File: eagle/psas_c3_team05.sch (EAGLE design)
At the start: 92 parts, among them IC1 CP2102, J1 3220-10-0100-00, J2 1.27MM_HDR_2X12X1, U1 MIC5319 3.3V, U2 MCP73871, U3 MKW01Z128, X1 32 MHz

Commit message: added attributes to battery connector, tri color LEDS
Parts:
- JP1: DIST (none) -> Digi-Key; DPN (none) -> 455-1749-1-ND; MFG (none) -> JST Sales America Inc.; MFG-PN (none) -> S2B-PH-SM4-TB(LF)(SN)
- LED1, LED2: DIST (none) -> Digi-Key; DPN 754-1100-1-ND -> 160-2022-1-ND; MFG (none) -> Lite-On Inc.; MFG-PN (none) -> LTST-C19FD1WT
- LED3: DIST (none) -> Digi-Key; MFG (none) -> Lite-On Inc.; MFG-PN (none) -> LTST-C191KGKT
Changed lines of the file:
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@@
 <attribute name="MFG-PN" value="MIC5319-3.3YD5-TR"/>
 </part>
-<part name="JP1" library="Vibrogait_prototype" deviceset="SPARKFUN-CONNECTORS_M02" device="4UCON-15767" value="BC"/>
+<part name="JP1" library="Vibrogait_prototype" deviceset="SPARKFUN-CONNECTORS_M02" device="4UCON-15767" value="BC">
+<attribute name="DIST" value="Digi-Key"/>
+<attribute name="DPN" value="455-1749-1-ND"/>
+<attribute name="MFG" value="JST Sales America Inc."/>
+<attribute name="MFG-PN" value="S2B-PH-SM4-TB(LF)(SN)"/>
+</part>
 <part name="GND1" library="Vibrogait_prototype" deviceset="GND" device=""/>
 <part name="RT1" library="Vibrogait_prototype" deviceset="THERMISTOR-" device="_1206" value="10K (NTC)">
@@
 <part name="GND25" library="Vibrogait_prototype" deviceset="GND" device=""/>
 <part name="LED1" library="Vibrogait_prototype" deviceset="LED_RGB_COMMON_ANODE-*" device="1.6X1.26" value="APHFT1612PBASURKVGAC">
-<attribute name="DPN" value="754-1100-1-ND"/>
+<attribute name="DIST" value="Digi-Key"/>
+<attribute name="DPN" value="160-2022-1-ND"/>
+<attribute name="MFG" value="Lite-On Inc."/>
+<attribute name="MFG-PN" value="LTST-C19FD1WT"/>
 </part>
 <part name="R3" library="rcl_custom" deviceset="R-US_" device="0603-B-NOSILK" value="1k">
@@
 <part name="TP18" library="microbuilder" deviceset="TESTPOINT" device="ROUND0.5MM"/>
 <part name="LED2" library="Vibrogait_prototype" deviceset="LED_RGB_COMMON_ANODE-*" device="1.6X1.26" value="APHFT1612PBASURKVGAC">
-<attribute name="DPN" value="754-1100-1-ND"/>
+<attribute name="DIST" value="Digi-Key"/>
+<attribute name="DPN" value="160-2022-1-ND"/>
+<attribute name="MFG" value="Lite-On Inc."/>
+<attribute name="MFG-PN" value="LTST-C19FD1WT"/>
 </part>
 <part name="LED3" library="Vibrogait_prototype" deviceset="LED" device="-0603" value="GRN">
+<attribute name="DIST" value="Digi-Key"/>
 <attribute name="DPN" value="160-1446-1-ND"/>
+<attribute name="MFG" value="Lite-On Inc."/>
+<attribute name="MFG-PN" value="LTST-C191KGKT"/>
 </part>
 <part name="R2" library="rcl_custom" deviceset="R-US_" device="0603-B-NOSILK" value="1k">
@@
 <attribute name="VALUE" x="347.98" y="332.74" size="1.778" layer="96" rot="MR0"/>
 <attribute name="NAME" x="347.98" y="343.662" size="1.778" layer="95" rot="MR0"/>
+<attribute name="DIST" x="345.44" y="337.82" size="1.778" layer="96" rot="MR0" display="off"/>
+<attribute name="DPN" x="345.44" y="337.82" size="1.778" layer="96" rot="MR0" display="off"/>
+<attribute name="MFG" x="345.44" y="337.82" size="1.778" layer="96" rot="MR0" display="off"/>
+<attribute name="MFG-PN" x="345.44" y="337.82" size="1.778" layer="96" rot="MR0" display="off"/>
 </instance>
 <instance part="GND1" gate="1" x="337.82" y="307.34" smashed="yes">
@@
 <attribute name="VALUE" x="210.82" y="320.04" size="1.778" layer="96"/>
 <attribute name="DPN" x="213.36" y="309.88" size="1.778" layer="96" rot="MR270" display="off"/>
+<attribute name="DIST" x="213.36" y="309.88" size="1.778" layer="96" rot="MR270" display="off"/>
+<attribute name="MFG" x="213.36" y="309.88" size="1.778" layer="96" rot="MR270" display="off"/>
+<attribute name="MFG-PN" x="213.36" y="309.88" size="1.778" layer="96" rot="MR270" display="off"/>
 </instance>
 <instance part="R3" gate="R" x="226.06" y="314.96" smashed="yes" rot="MR0">
@@
 <attribute name="VALUE" x="76.2" y="233.68" size="1.778" layer="96"/>
 <attribute name="DPN" x="119.38" y="233.68" size="1.778" layer="96" rot="MR0" display="off"/>
+<attribute name="DIST" x="119.38" y="233.68" size="1.778" layer="96" rot="MR0" display="off"/>
+<attribute name="MFG" x="119.38" y="233.68" size="1.778" layer="96" rot="MR0" display="off"/>
+<attribute name="MFG-PN" x="119.38" y="233.68" size="1.778" layer="96" rot="MR0" display="off"/>
 </instance>
 <instance part="LED3" gate="LED" x="477.52" y="345.44" smashed="yes">
@@
 <attribute name="VALUE" x="480.06" y="344.17" size="1.778" layer="96"/>
 <attribute name="DPN" x="477.52" y="345.44" size="1.778" layer="96" display="off"/>
+<attribute name="DIST" x="477.52" y="345.44" size="1.778" layer="96" display="off"/>
+<attribute name="MFG" x="477.52" y="345.44" size="1.778" layer="96" display="off"/>
+<attribute name="MFG-PN" x="477.52" y="345.44" size="1.778" layer="96" display="off"/>
 </instance>
 <instance part="R2" gate="R" x="477.52" y="337.82" smashed="yes" rot="R90">

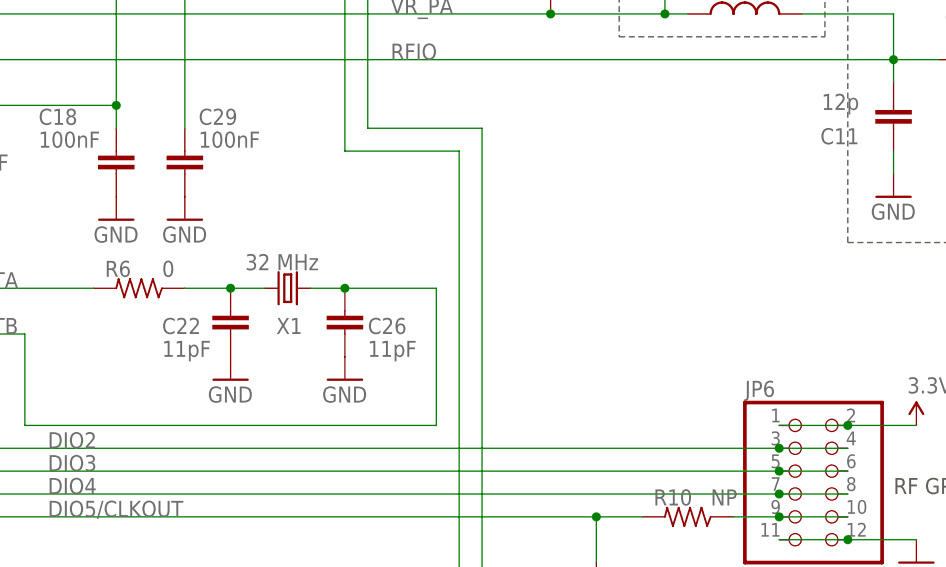
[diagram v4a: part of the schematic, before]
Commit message: added more attributes for part numbers, duplicated crystal because crystal footprint is wrong on the board and we will need to order two just in case things go wrong with the first, hopefully one of the two work lol
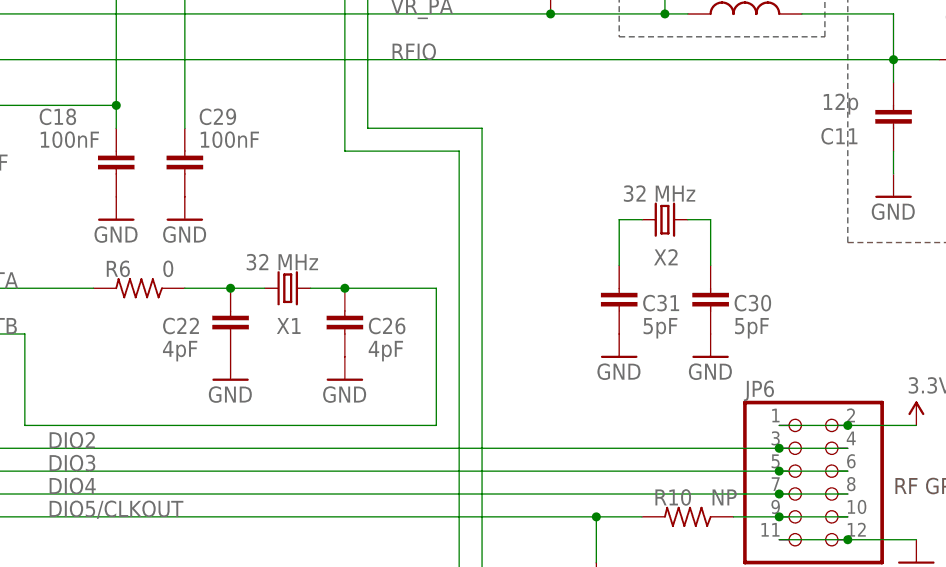
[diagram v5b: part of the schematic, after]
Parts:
- added C30, C31: 5pF, Vibrogait_prototype:C-EU0603-B-NOSILK
- added X2: 32 MHz, crystal:FC-12M
- C22, C26: value 11pF -> 4pF; DPN 490-1532-1-ND -> 490-10720-6-ND; MPN GRM188R71C104KA01D -> GRM1885C1H4R0CA01D
- X1: DPN2 CTX1364CT-ND -> (none); MFG2 CTS-Frequency Controls -> (none); MFG2-PN 402F3201XIAR -> (none)
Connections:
- new net N$14: C31.1, X2.2
- new net N$16: C30.1, X2.1
- net GND: now also C30.2, C31.2
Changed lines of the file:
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@@
 <setting verticaltext="up"/>
 </settings>
-<grid distance="0.1" unitdist="inch" unit="inch" style="lines" multiple="1" display="no" altdistance="0.01" altunitdist="inch" altunit="inch"/>
+<grid distance="0.05" unitdist="inch" unit="inch" style="lines" multiple="1" display="no" altdistance="0.01" altunitdist="inch" altunit="inch"/>
 <layers>
 <layer number="1" name="Top" color="4" fill="1" visible="no" active="no"/>
@@
 <attribute name="DIST" value="Digi-Key"/>
 <attribute name="DPN" value="1253-1161-1-ND"/>
-<attribute name="DPN2" value="CTX1364CT-ND"/>
 <attribute name="MFG" value="AVX Corp/Kyocera Corp"/>
 <attribute name="MFG-PN" value="CX3225GA32000D0PTVCC"/>
-<attribute name="MFG2" value="CTS-Frequency Controls"/>
-<attribute name="MFG2-PN" value="402F3201XIAR"/>
 </part>
 <part name="R6" library="rcl_custom" deviceset="R-US_" device="0603-B-NOSILK" value="0"/>
-<part name="C22" library="Vibrogait_prototype" deviceset="C-EU" device="0603-B-NOSILK" value="11pF">
-<attribute name="DIST" value="Digi-Key"/>
-<attribute name="DPN" value="490-1532-1-ND"/>
+<part name="C22" library="Vibrogait_prototype" deviceset="C-EU" device="0603-B-NOSILK" value="4pF">
+<attribute name="DIST" value="Digi-Key"/>
+<attribute name="DPN" value="490-10720-6-ND"/>
 <attribute name="MFG" value="Murata Electronics North America"/>
-<attribute name="MPN" value="GRM188R71C104KA01D"/>
-</part>
-<part name="C26" library="Vibrogait_prototype" deviceset="C-EU" device="0603-B-NOSILK" value="11pF">
-<attribute name="DIST" value="Digi-Key"/>
-<attribute name="DPN" value="490-1532-1-ND"/>
+<attribute name="MPN" value="GRM1885C1H4R0CA01D"/>
+</part>
+<part name="C26" library="Vibrogait_prototype" deviceset="C-EU" device="0603-B-NOSILK" value="4pF">
+<attribute name="DIST" value="Digi-Key"/>
+<attribute name="DPN" value="490-10720-6-ND"/>
 <attribute name="MFG" value="Murata Electronics North America"/>
-<attribute name="MPN" value="GRM188R71C104KA01D"/>
+<attribute name="MPN" value="GRM1885C1H4R0CA01D"/>
 </part>
 <part name="GND28" library="Vibrogait_prototype" deviceset="GND" device=""/>
@@
 <attribute name="MFG-PN" value="LQW18AN15NG00D"/>
 </part>
+<part name="X2" library="crystal" deviceset="FC-12M" device="" value="32 MHz">
+<attribute name="DIST" value="Digi-Key"/>
+<attribute name="DPN" value="CTX1364CT-ND"/>
+<attribute name="MFG" value="CTS-Frequency Controls"/>
+<attribute name="MFG-PN" value="402F3201XIAR"/>
+</part>
+<part name="C30" library="Vibrogait_prototype" deviceset="C-EU" device="0603-B-NOSILK" value="5pF">
+<attribute name="DIST" value="Digi-Key"/>
+<attribute name="DPN" value="490-10720-6-ND"/>
+<attribute name="MFG" value="Murata Electronics North America"/>
+<attribute name="MPN" value="GRM1885C1H4R0CA01D"/>
+</part>
+<part name="C31" library="Vibrogait_prototype" deviceset="C-EU" device="0603-B-NOSILK" value="5pF">
+<attribute name="DIST" value="Digi-Key"/>
+<attribute name="DPN" value="490-10720-6-ND"/>
+<attribute name="MFG" value="Murata Electronics North America"/>
+<attribute name="MPN" value="GRM1885C1H4R0CA01D"/>
+</part>
+<part name="GND45" library="Vibrogait_prototype" deviceset="GND" device=""/>
+<part name="GND46" library="Vibrogait_prototype" deviceset="GND" device=""/>
 </parts>
 <sheets>
@@
 <attribute name="MFG" x="328.93" y="193.04" size="1.778" layer="96" rot="R180" display="off"/>
 <attribute name="MFG-PN" x="328.93" y="193.04" size="1.778" layer="96" rot="R180" display="off"/>
-<attribute name="DPN2" x="328.93" y="193.04" size="1.778" layer="96" rot="R180" display="off"/>
-<attribute name="MFG2" x="328.93" y="193.04" size="1.778" layer="96" rot="R180" display="off"/>
-<attribute name="MFG2-PN" x="328.93" y="193.04" size="1.778" layer="96" rot="R180" display="off"/>
 </instance>
 <instance part="R6" gate="R" x="312.42" y="193.04" smashed="yes" rot="R180">
@@
 <attribute name="MFG" x="447.04" y="218.44" size="1.778" layer="96" display="off"/>
 <attribute name="MFG-PN" x="447.04" y="218.44" size="1.778" layer="96" display="off"/>
+</instance>
+<instance part="X2" gate="G$1" x="370.84" y="200.66" smashed="yes" rot="R180">
+<attribute name="NAME" x="369.57" y="195.58" size="1.778" layer="95"/>
+<attribute name="VALUE" x="366.1156" y="202.6666" size="1.778" layer="96"/>
+<attribute name="DIST" x="370.84" y="200.66" size="1.778" layer="96" rot="R180" display="off"/>
+<attribute name="DPN" x="370.84" y="200.66" size="1.778" layer="96" rot="R180" display="off"/>
+<attribute name="MFG" x="370.84" y="200.66" size="1.778" layer="96" rot="R180" display="off"/>
+<attribute name="MFG-PN" x="370.84" y="200.66" size="1.778" layer="96" rot="R180" display="off"/>
+</instance>
+<instance part="C30" gate="CE" x="375.92" y="193.04" smashed="yes">
+<attribute name="DIST" x="375.92" y="193.04" size="1.778" layer="96" display="off"/>
+<attribute name="DPN" x="375.92" y="193.04" size="1.778" layer="96" display="off"/>
+<attribute name="MFG" x="375.92" y="193.04" size="1.778" layer="96" display="off"/>
+<attribute name="MPN" x="375.92" y="193.04" size="1.778" layer="96" display="off"/>
+<attribute name="NAME" x="378.46" y="190.5" size="1.778" layer="95"/>
+<attribute name="VALUE" x="378.46" y="187.96" size="1.778" layer="96"/>
+</instance>
+<instance part="C31" gate="CE" x="365.76" y="193.04" smashed="yes">
+<attribute name="DIST" x="365.76" y="193.04" size="1.778" layer="96" display="off"/>
+<attribute name="DPN" x="365.76" y="193.04" size="1.778" layer="96" display="off"/>
+<attribute name="MFG" x="365.76" y="193.04" size="1.778" layer="96" display="off"/>
+<attribute name="MPN" x="365.76" y="193.04" size="1.778" layer="96" display="off"/>
+<attribute name="NAME" x="368.3" y="190.5" size="1.778" layer="95"/>
+<attribute name="VALUE" x="368.3" y="187.96" size="1.778" layer="96"/>
+</instance>
+<instance part="GND45" gate="1" x="365.76" y="185.42" smashed="yes">
+<attribute name="VALUE" x="363.22" y="182.88" size="1.778" layer="96"/>
+</instance>
+<instance part="GND46" gate="1" x="375.92" y="185.42" smashed="yes">
+<attribute name="VALUE" x="373.38" y="182.88" size="1.778" layer="96"/>
 </instance>
 </instances>
@@
 <wire x1="500.38" y1="297.18" x2="492.76" y2="297.18" width="0.1524" layer="91"/>
 <wire x1="492.76" y1="297.18" x2="492.76" y2="294.64" width="0.1524" layer="91"/>
+</segment>
+<segment>
+<pinref part="C31" gate="CE" pin="2"/>
+<pinref part="GND45" gate="1" pin="GND"/>
+</segment>
+<segment>
+<pinref part="C30" gate="CE" pin="2"/>
+<pinref part="GND46" gate="1" pin="GND"/>
 </segment>
 </net>
@@
 </segment>
 </net>
+<net name="N$14" class="0">
+<segment>
+<pinref part="C31" gate="CE" pin="1"/>
+<wire x1="365.76" y1="195.58" x2="365.76" y2="200.66" width="0.1524" layer="91"/>
+<pinref part="X2" gate="G$1" pin="2"/>
+<wire x1="365.76" y1="200.66" x2="368.3" y2="200.66" width="0.1524" layer="91"/>
+</segment>
+</net>
+<net name="N$16" class="0">
+<segment>
+<pinref part="C30" gate="CE" pin="1"/>
+<wire x1="375.92" y1="195.58" x2="375.92" y2="200.66" width="0.1524" layer="91"/>
+<wire x1="375.92" y1="200.66" x2="373.38" y2="200.66" width="0.1524" layer="91"/>
+<pinref part="X2" gate="G$1" pin="1"/>
+</segment>
+</net>

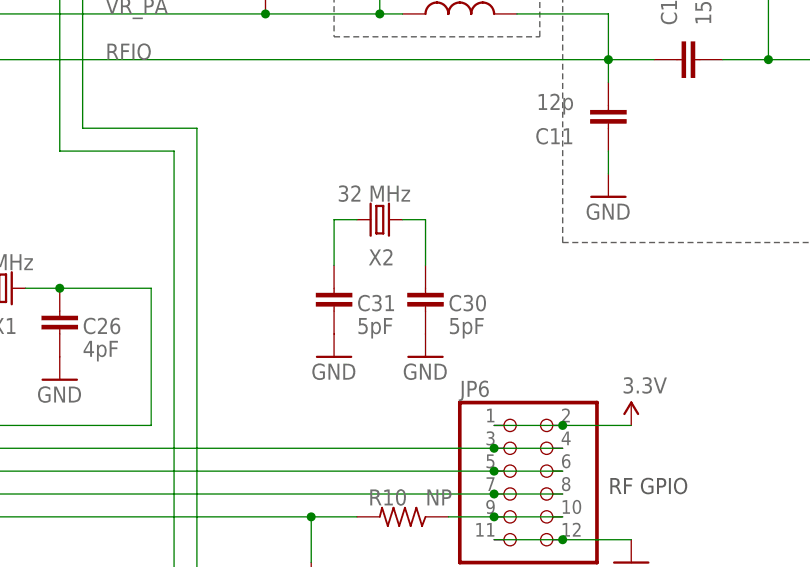
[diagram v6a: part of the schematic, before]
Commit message: took extra crystal off schematic, corrected bogus airwire
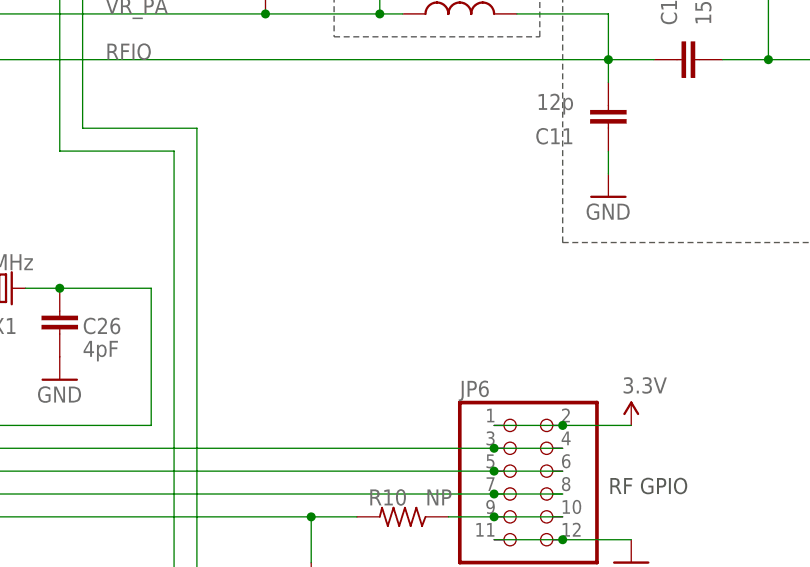
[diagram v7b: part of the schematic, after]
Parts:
- removed C30, C31: 5pF, Vibrogait_prototype:C-EU0603-B-NOSILK
- removed X2: 32 MHz, crystal:FC-12M
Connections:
- removed net N$14: C31.1, X2.2
- removed net N$16: C30.1, X2.1
- net GND: no longer C30.2, C31.2
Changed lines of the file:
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@@
 <?xml version="1.0" encoding="utf-8"?>
 <!DOCTYPE eagle SYSTEM "eagle.dtd">
-<eagle version="7.4.0">
+<eagle version="7.3.0">
 <drawing>
 <settings>
@@
 <attribute name="MFG-PN" value="LQW18AN15NG00D"/>
 </part>
-<part name="X2" library="crystal" deviceset="FC-12M" device="" value="32 MHz">
-<attribute name="DIST" value="Digi-Key"/>
-<attribute name="DPN" value="CTX1364CT-ND"/>
-<attribute name="MFG" value="CTS-Frequency Controls"/>
-<attribute name="MFG-PN" value="402F3201XIAR"/>
-</part>
-<part name="C30" library="Vibrogait_prototype" deviceset="C-EU" device="0603-B-NOSILK" value="5pF">
-<attribute name="DIST" value="Digi-Key"/>
-<attribute name="DPN" value="490-10720-6-ND"/>
-<attribute name="MFG" value="Murata Electronics North America"/>
-<attribute name="MPN" value="GRM1885C1H4R0CA01D"/>
-</part>
-<part name="C31" library="Vibrogait_prototype" deviceset="C-EU" device="0603-B-NOSILK" value="5pF">
-<attribute name="DIST" value="Digi-Key"/>
-<attribute name="DPN" value="490-10720-6-ND"/>
-<attribute name="MFG" value="Murata Electronics North America"/>
-<attribute name="MPN" value="GRM1885C1H4R0CA01D"/>
-</part>
-<part name="GND45" library="Vibrogait_prototype" deviceset="GND" device=""/>
-<part name="GND46" library="Vibrogait_prototype" deviceset="GND" device=""/>
 </parts>
 <sheets>
@@
 <attribute name="MFG-PN" x="447.04" y="218.44" size="1.778" layer="96" display="off"/>
 </instance>
-<instance part="X2" gate="G$1" x="370.84" y="200.66" smashed="yes" rot="R180">
-<attribute name="NAME" x="369.57" y="195.58" size="1.778" layer="95"/>
-<attribute name="VALUE" x="366.1156" y="202.6666" size="1.778" layer="96"/>
-<attribute name="DIST" x="370.84" y="200.66" size="1.778" layer="96" rot="R180" display="off"/>
-<attribute name="DPN" x="370.84" y="200.66" size="1.778" layer="96" rot="R180" display="off"/>
-<attribute name="MFG" x="370.84" y="200.66" size="1.778" layer="96" rot="R180" display="off"/>
-<attribute name="MFG-PN" x="370.84" y="200.66" size="1.778" layer="96" rot="R180" display="off"/>
-</instance>
-<instance part="C30" gate="CE" x="375.92" y="193.04" smashed="yes">
-<attribute name="DIST" x="375.92" y="193.04" size="1.778" layer="96" display="off"/>
-<attribute name="DPN" x="375.92" y="193.04" size="1.778" layer="96" display="off"/>
-<attribute name="MFG" x="375.92" y="193.04" size="1.778" layer="96" display="off"/>
-<attribute name="MPN" x="375.92" y="193.04" size="1.778" layer="96" display="off"/>
-<attribute name="NAME" x="378.46" y="190.5" size="1.778" layer="95"/>
-<attribute name="VALUE" x="378.46" y="187.96" size="1.778" layer="96"/>
-</instance>
-<instance part="C31" gate="CE" x="365.76" y="193.04" smashed="yes">
-<attribute name="DIST" x="365.76" y="193.04" size="1.778" layer="96" display="off"/>
-<attribute name="DPN" x="365.76" y="193.04" size="1.778" layer="96" display="off"/>
-<attribute name="MFG" x="365.76" y="193.04" size="1.778" layer="96" display="off"/>
-<attribute name="MPN" x="365.76" y="193.04" size="1.778" layer="96" display="off"/>
-<attribute name="NAME" x="368.3" y="190.5" size="1.778" layer="95"/>
-<attribute name="VALUE" x="368.3" y="187.96" size="1.778" layer="96"/>
-</instance>
-<instance part="GND45" gate="1" x="365.76" y="185.42" smashed="yes">
-<attribute name="VALUE" x="363.22" y="182.88" size="1.778" layer="96"/>
-</instance>
-<instance part="GND46" gate="1" x="375.92" y="185.42" smashed="yes">
-<attribute name="VALUE" x="373.38" y="182.88" size="1.778" layer="96"/>
-</instance>
 </instances>
 <busses>
@@
 <wire x1="500.38" y1="297.18" x2="492.76" y2="297.18" width="0.1524" layer="91"/>
 <wire x1="492.76" y1="297.18" x2="492.76" y2="294.64" width="0.1524" layer="91"/>
-</segment>
-<segment>
-<pinref part="C31" gate="CE" pin="2"/>
-<pinref part="GND45" gate="1" pin="GND"/>
-</segment>
-<segment>
-<pinref part="C30" gate="CE" pin="2"/>
-<pinref part="GND46" gate="1" pin="GND"/>
 </segment>
 </net>
@@
 </segment>
 </net>
-<net name="N$14" class="0">
-<segment>
-<pinref part="C31" gate="CE" pin="1"/>
-<wire x1="365.76" y1="195.58" x2="365.76" y2="200.66" width="0.1524" layer="91"/>
-<pinref part="X2" gate="G$1" pin="2"/>
-<wire x1="365.76" y1="200.66" x2="368.3" y2="200.66" width="0.1524" layer="91"/>
-</segment>
-</net>
-<net name="N$16" class="0">
-<segment>
-<pinref part="C30" gate="CE" pin="1"/>
-<wire x1="375.92" y1="195.58" x2="375.92" y2="200.66" width="0.1524" layer="91"/>
-<wire x1="375.92" y1="200.66" x2="373.38" y2="200.66" width="0.1524" layer="91"/>
-<pinref part="X2" gate="G$1" pin="1"/>
-</segment>
-</net>
